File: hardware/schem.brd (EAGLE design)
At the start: 66.3 x 45.7 mm, 9 parts, among them IC1 7805L, U1 ATTINY85-P

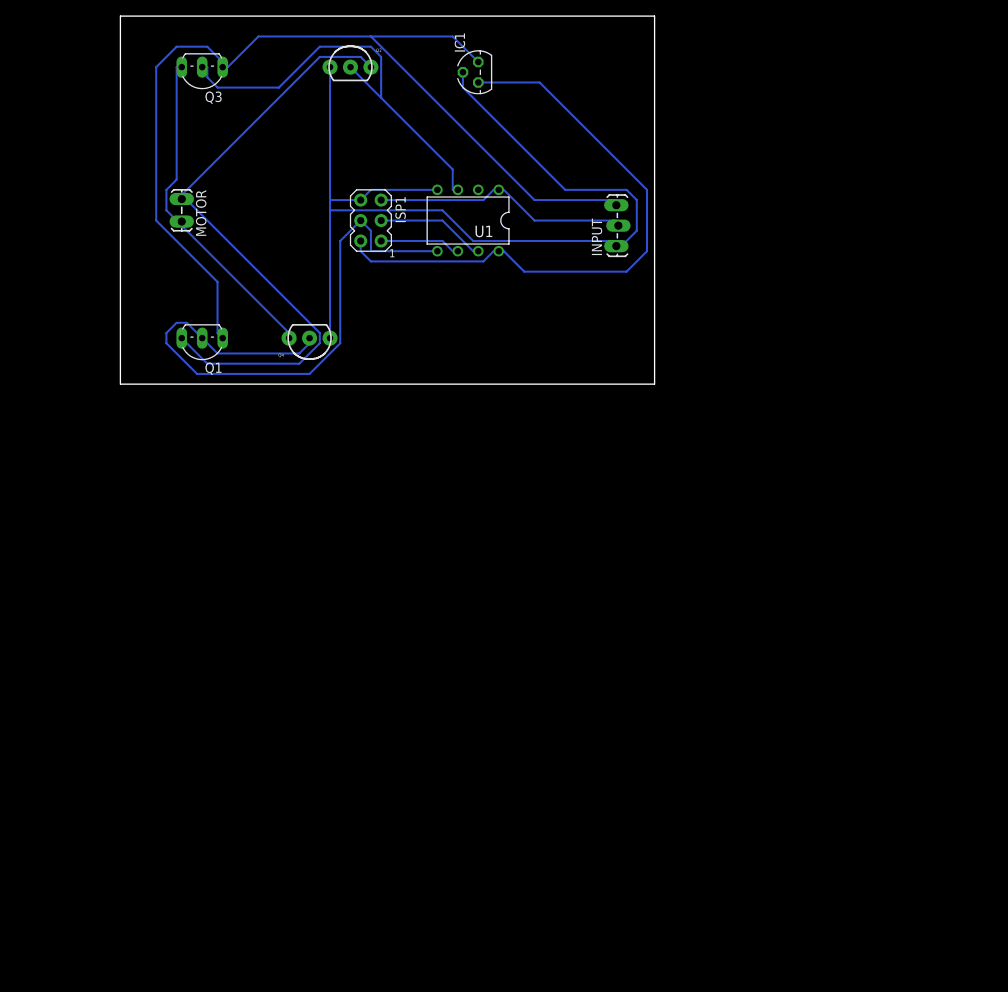
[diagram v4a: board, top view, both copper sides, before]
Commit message: selencetd new mosfets and routed
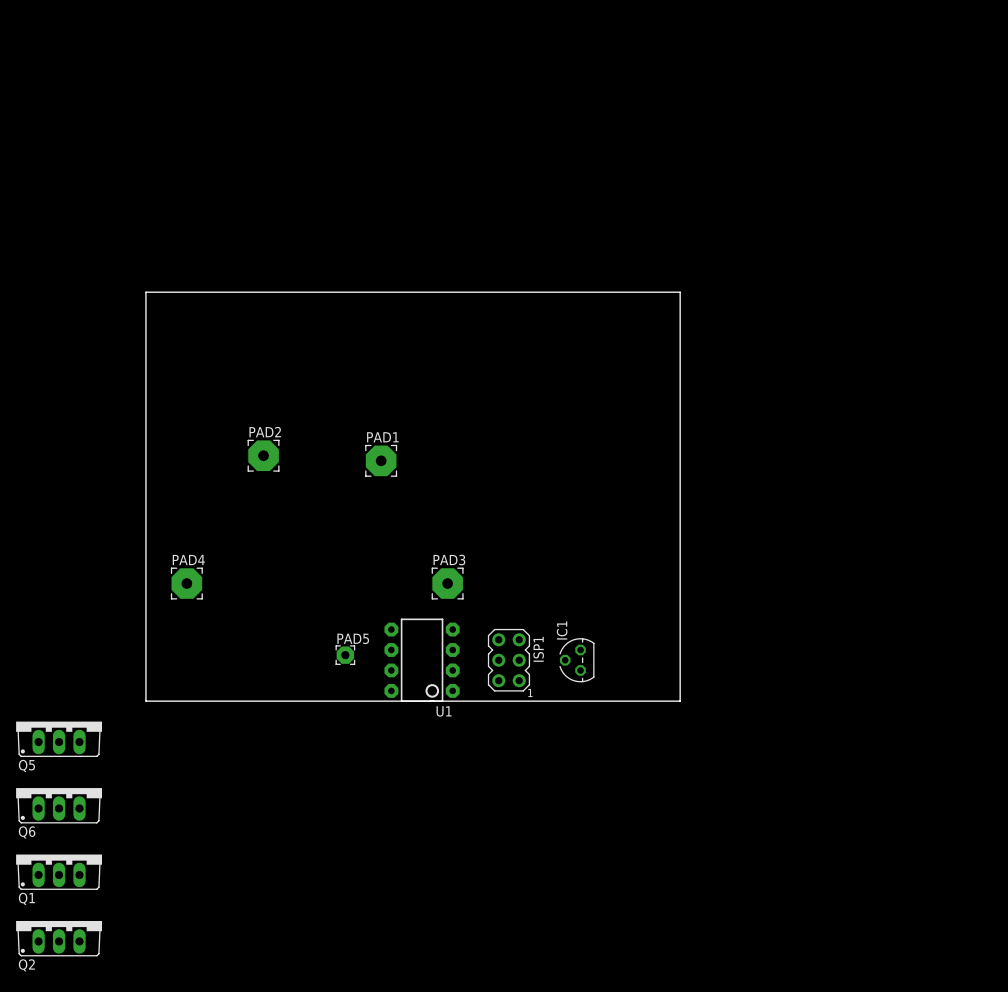
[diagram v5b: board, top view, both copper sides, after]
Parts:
- removed INPUT: (no value), SparkFun-Connectors:1X03_LOCK_LONGPADS
- removed MOTOR: M02LOCK_LONGPADS, SparkFun-Connectors:1X02_LOCK_LONGPADS
- removed Q3: (no value), transistor:TO92-EBC
- removed Q4: (no value), SparkFun-DiscreteSemi:TO-92-AMMO
- added PAD1, PAD2, PAD3, PAD4: (no value), wirepad:3,81/1,3
- added PAD5: (no value), wirepad:2,15/1,0
- added Q5, Q6: IRF9530, transistor-power:TO220BV
- Q1: value (none) -> IRF512; device transistor:TO92-EBC -> transistor-power:TO220BV
- Q2: value (none) -> IRF512; device SparkFun-DiscreteSemi:TO-92-AMMO -> transistor-power:TO220BV
- U1: value ATTINY85-P -> TINY45-20-DIP; device _hhn_attiny25_45_85:PDIP08_300MIL -> SparkFun-DigitalIC:DIP08
- moved Q2 112.1 mm to (-10.8, -27.3)
- moved IC1 74.1 mm to (54.0, 5.08)
- moved Q1 65.3 mm to (-10.8, -19.1), turned to 0 degrees
- moved ISP1 57.2 mm to (45.1, 5.08)
- moved U1 54.9 mm to (34.3, 5.08), turned to 90 degrees
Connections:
- net +12V: now also PAD3.1, Q5.S, Q6.S; no longer INPUT.3, Q1.E, Q3.E
- net GND: now also PAD4.1, Q1.S, Q2.S; no longer INPUT.1, Q2.1, Q4.1
- net INP: now also PAD5.1, U1.5; no longer INPUT.2, U1.1
- net MISO: now also Q1.G, Q6.G, U1.3; no longer U1.6
- net MOSI: now also U1.1; no longer Q1.B, Q4.2, U1.5
- net N$1: now also PAD1.1, Q1.D, Q5.D; no longer MOTOR.1, Q1.C, Q2.3
- net N$2: now also PAD2.1, Q2.D, Q6.D; no longer MOTOR.2, Q3.C, Q4.3
- net OUT: now also Q2.G, Q5.G, U1.6; no longer Q2.2, Q3.B, U1.3
- net SCK: now also U1.2; no longer U1.7
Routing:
- net GND: track 122.6 -> 0.00 mm
- net +12V: track 122.2 -> 0.00 mm
- net N$1: track 77.4 -> 0.00 mm
- net MOSI: track 75.9 -> 0.00 mm
- net +5V: track 74.1 -> 0.00 mm
- net OUT: track 52.9 -> 0.00 mm
- net N$2: track 41.8 -> 0.00 mm
- net INP: track 32.0 -> 0.00 mm
- net SCK: track 13.6 -> 0.00 mm
- net MISO: track 10.1 -> 0.00 mm
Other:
- board size 66.3 x 45.7 mm -> 66.3 x 50.8 mm

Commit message: added large ground plane and power supply capacitors
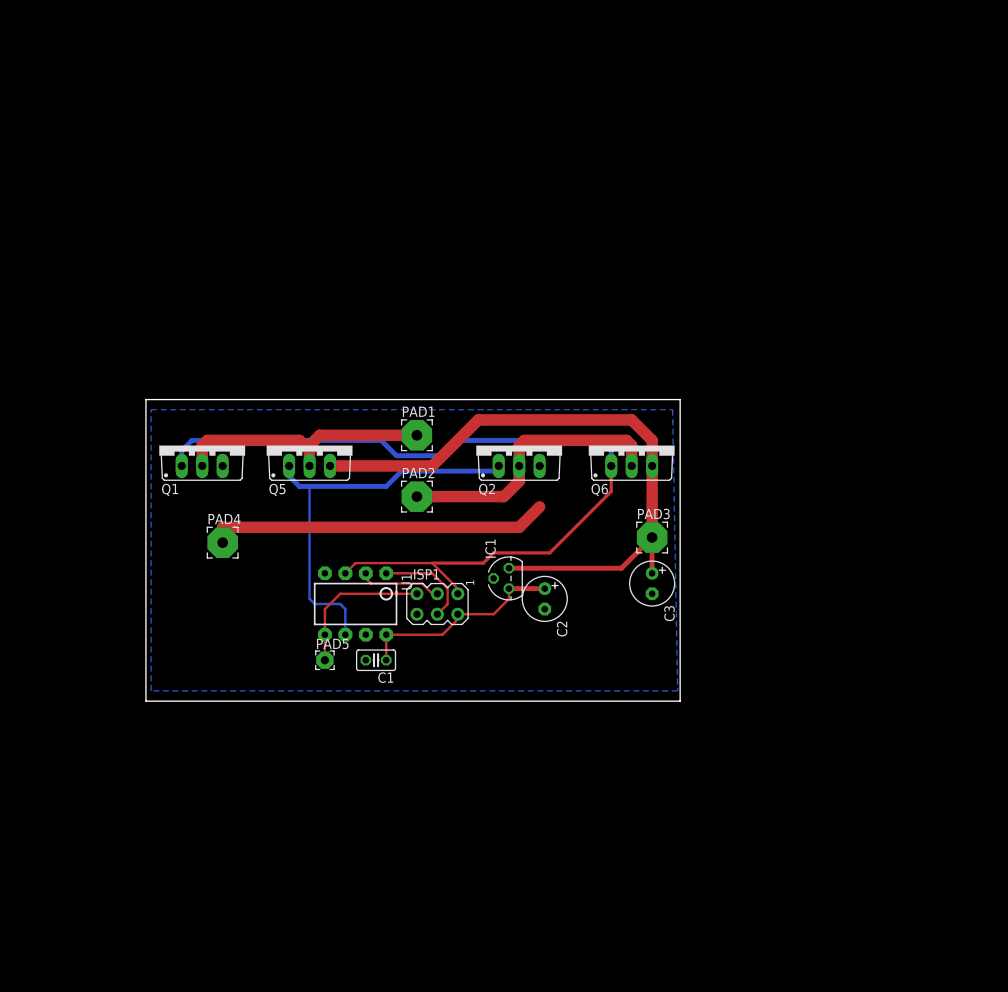
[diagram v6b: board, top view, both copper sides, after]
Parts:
- added C1: (no value), rcl:C025-025X050
- added C2, C3: (no value), rcl:E2,5-6
- moved Q6 82.9 mm to (60.3, 31.8)
- moved Q2 82.2 mm to (46.4, 31.8)
- moved Q1 53.8 mm to (6.99, 31.8)
- moved Q5 46.3 mm to (20.3, 31.8)
- moved PAD3 26.0 mm to (62.9, 20.3)
- moved PAD2 19.7 mm to (33.7, 25.4)
- moved IC1 13.5 mm to (45.1, 15.2)
- moved ISP1 11.3 mm to (36.2, 12.1), turned to 270 degrees
- moved U1 10.8 mm to (26.0, 12.1), turned to 180 degrees
- moved PAD4 6.75 mm to (9.53, 19.7)
- moved PAD1 5.46 mm to (33.7, 33.0)
- moved PAD5 2.62 mm to (22.2, 5.08)
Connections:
- net +12V: now also C3.+
- net +5V: now also C1.1, C2.+
- net GND: now also C1.2, C2.-, C3.-
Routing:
- net MISO: track 0.00 -> 105.3 mm
- net +12V: track 0.00 -> 79.3 mm
- net OUT: track 0.00 -> 51.0 mm
- net GND: track 0.00 -> 42.3 mm
- net N$2: track 0.00 -> 35.0 mm
- net N$1: track 0.00 -> 33.1 mm
- net +5V: track 0.00 -> 26.3 mm
- net INP: track 0.00 -> 18.6 mm
- net MOSI: track 0.00 -> 12.1 mm
- net SCK: track 0.00 -> 10.3 mm
- added copper zone on layer 16, net GND
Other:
- board size 66.3 x 50.8 mm -> 66.3 x 37.5 mm

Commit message: Removed power transistor from ground plane
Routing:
- net GND: track 42.3 -> 55.0 mm
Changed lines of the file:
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@@
 <wire x1="46.355" y1="21.59" x2="9.525" y2="21.59" width="1.4224" layer="1"/>
 <polygon width="0.6096" layer="16" isolate="0.6604">
-<vertex x="0.635" y="36.195"/>
-<vertex x="65.405" y="36.195"/>
+<vertex x="0.635" y="25.4"/>
+<vertex x="65.405" y="26.035"/>
 <vertex x="66.04" y="1.27"/>
 <vertex x="0.635" y="1.27"/>
@@
 <contactref element="Q1" pad="S"/>
 <contactref element="Q2" pad="S"/>
+<wire x1="9.525" y1="29.21" x2="9.525" y2="21.59" width="1.4224" layer="1"/>
+<wire x1="48.895" y1="29.21" x2="48.895" y2="24.13" width="1.4224" layer="1"/>
 </signal>
 <signal name="+12V">

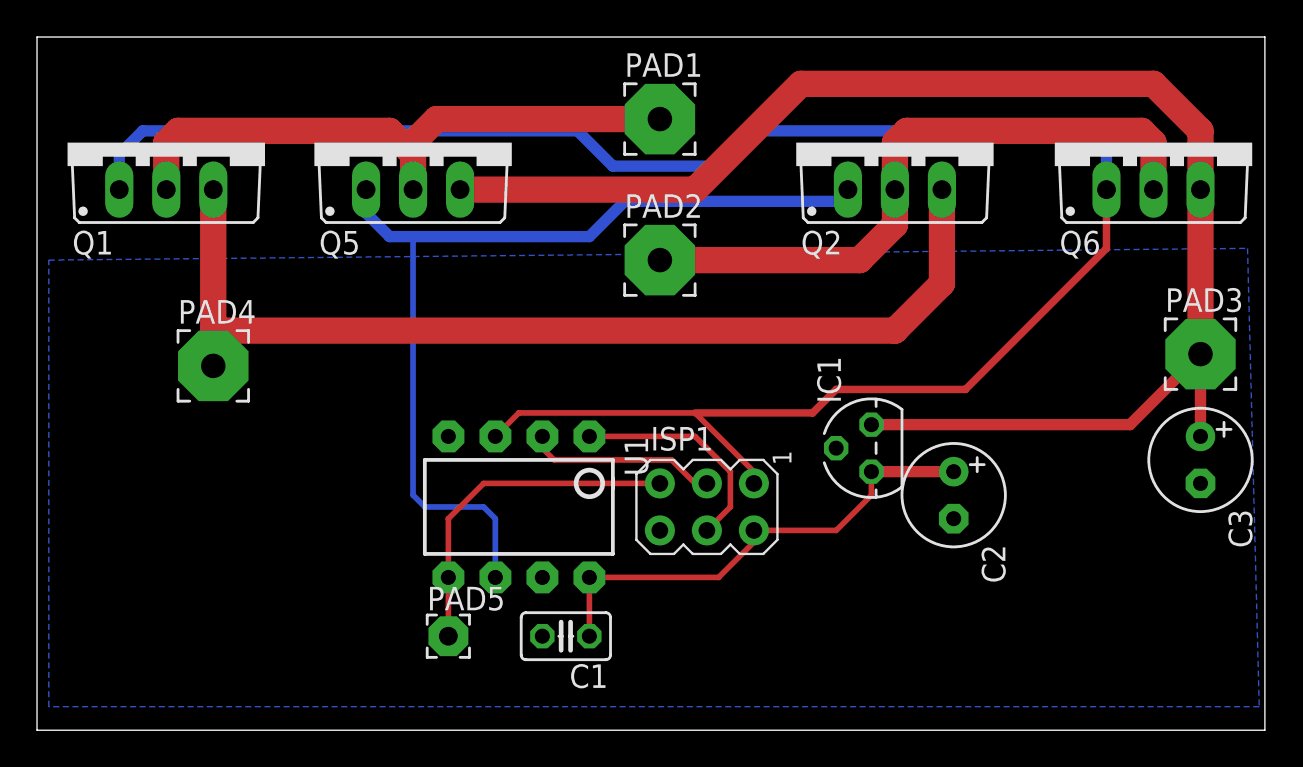
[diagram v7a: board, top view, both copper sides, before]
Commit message: modified silkscreen and worked on Power supply capacitor placement
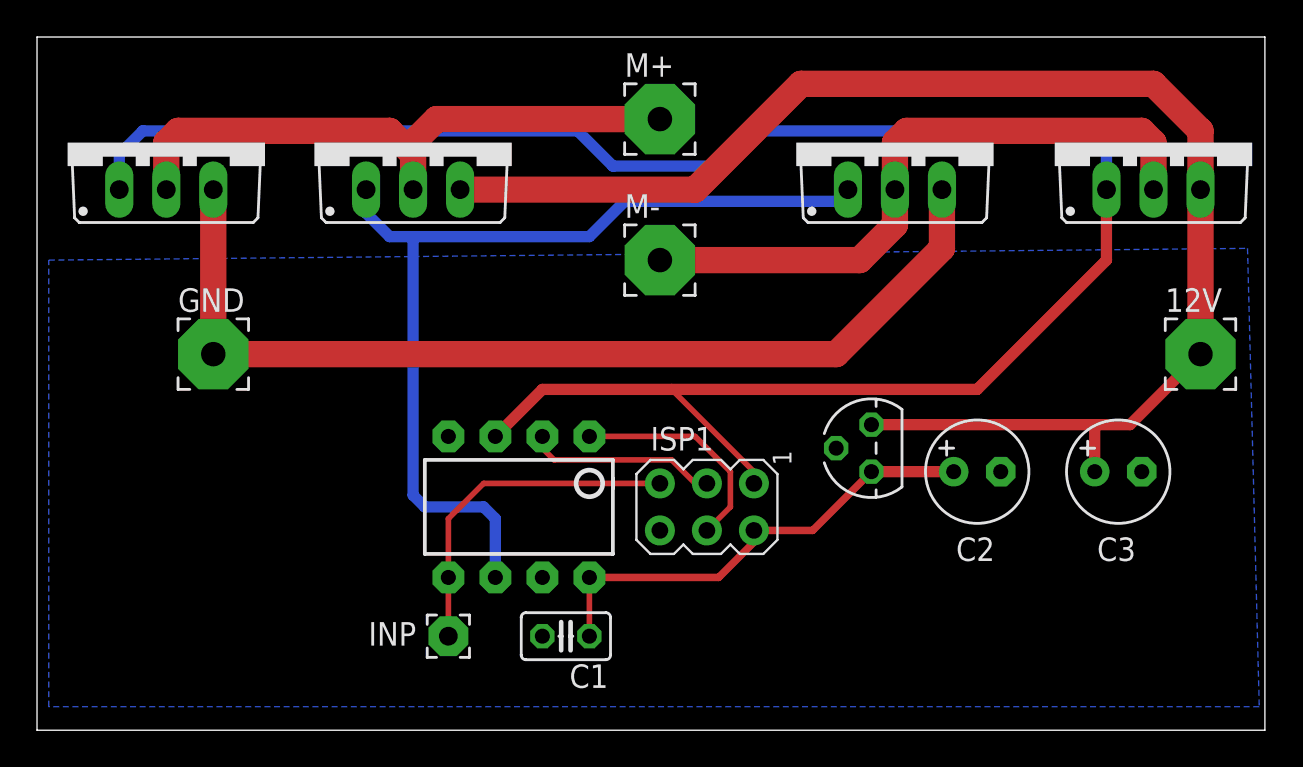
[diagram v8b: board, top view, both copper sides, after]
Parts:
- removed PAD4: (no value), wirepad:3,81/1,3
- added GND: (no value), wirepad:3,81/1,3
- INP: value (none) -> INP
- moved C3 4.49 mm to (58.4, 14.0), turned to 0 degrees
- moved C2 1.80 mm to (50.8, 14.0), turned to 0 degrees
- renumbered PAD1 to M+, PAD2 to M-, PAD3 to 12V, PAD5 to INP
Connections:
- net GND: now also GND.1; no longer PAD4.1
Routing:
- net MISO: track 105.3 -> 107.5 mm
- net +12V: track 79.3 -> 77.4 mm
- net GND: track 55.0 -> 53.8 mm
- net +5V: track 26.3 -> 25.6 mm
